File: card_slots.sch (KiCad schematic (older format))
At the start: 0 parts

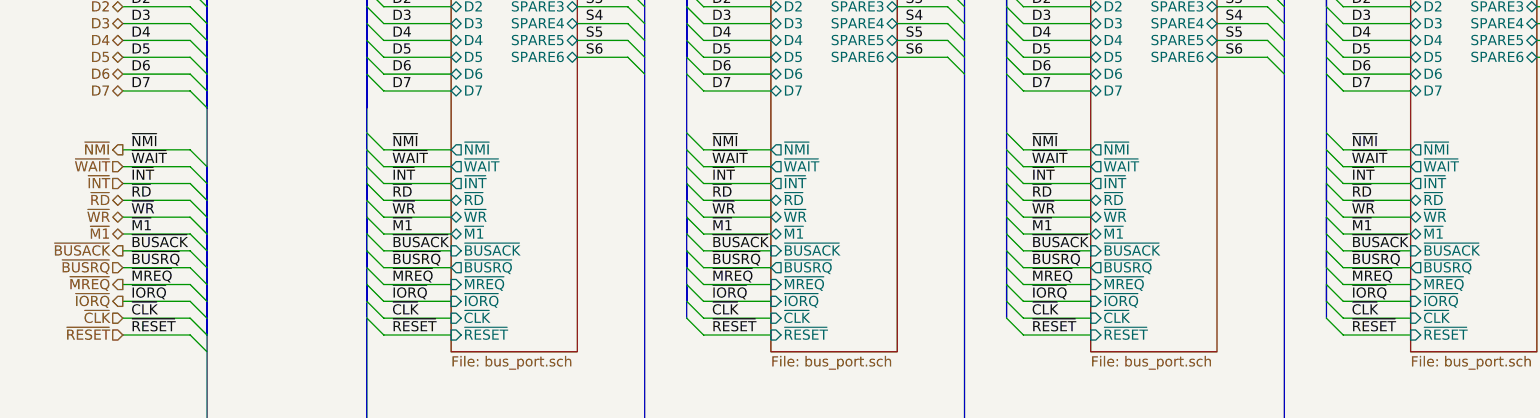
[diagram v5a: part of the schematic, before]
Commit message: Added /intack signal and a pri-encoder for /iosel
Brain fart on the diode crap. Was tired. Added a priority encoder to
enable the Dx buffer so it properly tristates when no IObus ports are
selected.

Added a NOR gate to provide a /intack signal for any board to properly
detect their interupt has been accepted but the z80. Boards will need to
figure out who the interupt is for.

Will have to add interupt priority pins to the boards to allow the
boards to put jump vectors onto the data bus to service the interrupt
This should be fairly easy, just means the service pritority of the
slots will be A-H, with A being the highest priority and H being the
lowest.

Going to replace the hex inverters with the spare NOR gates too.
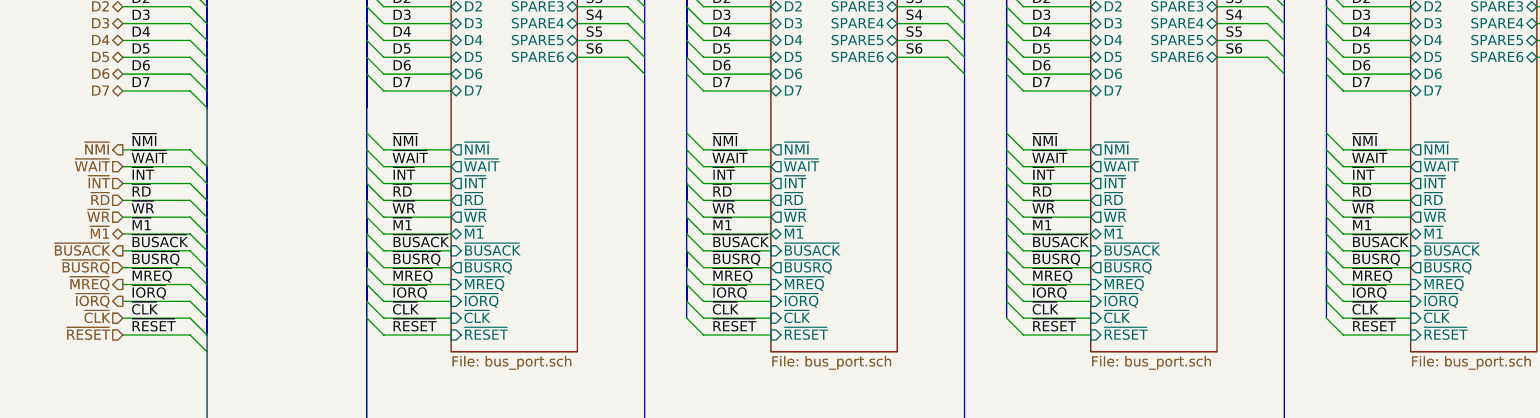
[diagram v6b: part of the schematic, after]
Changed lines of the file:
@@
 $Descr A4 11693 8268
 encoding utf-8
-Sheet 3 16
+Sheet 12 14
 Title ""
 Date ""
@@
 F26 "~WAIT" O L 3650 4750 60
 F27 "~INT" O L 3650 4850 60
-F28 "~RD" T L 3650 4950 60
-F29 "~WR" T L 3650 5050 60
+F28 "~RD" O L 3650 4950 60
+F29 "~WR" O L 3650 5050 60
 F30 "~M1" T L 3650 5150 60
 F31 "~BUSACK" I L 3650 5250 60
@@
 Text HLabel 1700 4850 0    60   Input ~ 0
 ~INT
-Text HLabel 1700 4950 0    60   3State ~ 0
+Text HLabel 1700 4950 0    60   Input ~ 0
 ~RD
-Text HLabel 1700 5050 0    60   3State ~ 0
+Text HLabel 1700 5050 0    60   Input ~ 0
 ~WR
 Text HLabel 1700 5150 0    60   3State ~ 0
@@
 F26 "~WAIT" O L 5550 4750 60
 F27 "~INT" O L 5550 4850 60
-F28 "~RD" T L 5550 4950 60
-F29 "~WR" T L 5550 5050 60
+F28 "~RD" O L 5550 4950 60
+F29 "~WR" O L 5550 5050 60
 F30 "~M1" T L 5550 5150 60
 F31 "~BUSACK" I L 5550 5250 60
@@
 F26 "~WAIT" O L 7450 4750 60
 F27 "~INT" O L 7450 4850 60
-F28 "~RD" T L 7450 4950 60
-F29 "~WR" T L 7450 5050 60
+F28 "~RD" O L 7450 4950 60
+F29 "~WR" O L 7450 5050 60
 F30 "~M1" T L 7450 5150 60
 F31 "~BUSACK" I L 7450 5250 60
@@
 F26 "~WAIT" O L 9350 4750 60
 F27 "~INT" O L 9350 4850 60
-F28 "~RD" T L 9350 4950 60
-F29 "~WR" T L 9350 5050 60
+F28 "~RD" O L 9350 4950 60
+F29 "~WR" O L 9350 5050 60
 F30 "~M1" T L 9350 5150 60
 F31 "~BUSACK" I L 9350 5250 60
